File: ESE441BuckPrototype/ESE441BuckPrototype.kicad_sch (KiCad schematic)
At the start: 0 parts

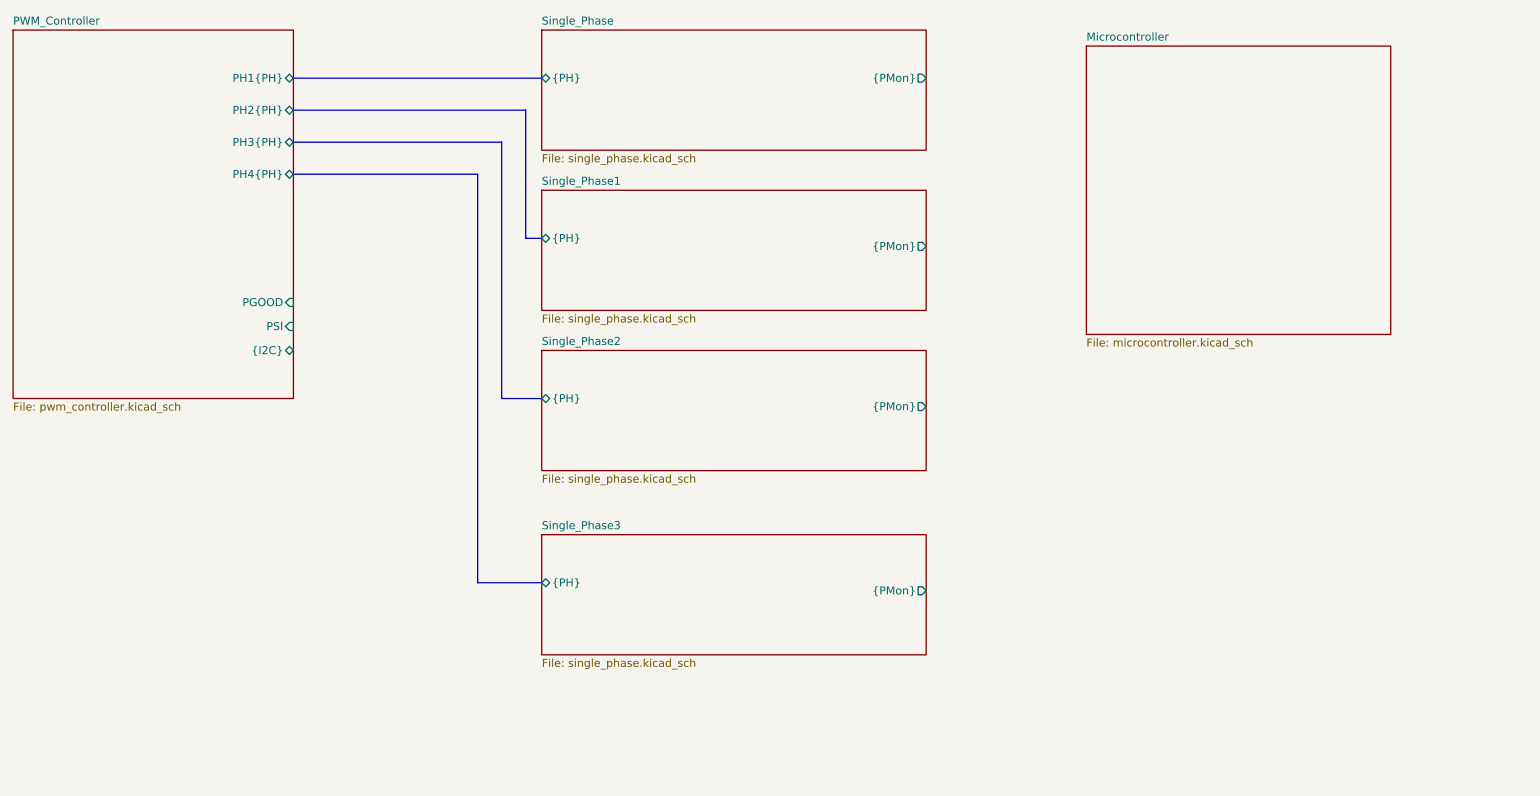
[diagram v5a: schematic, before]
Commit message: Wire up microcontroller to phases and PWM controller
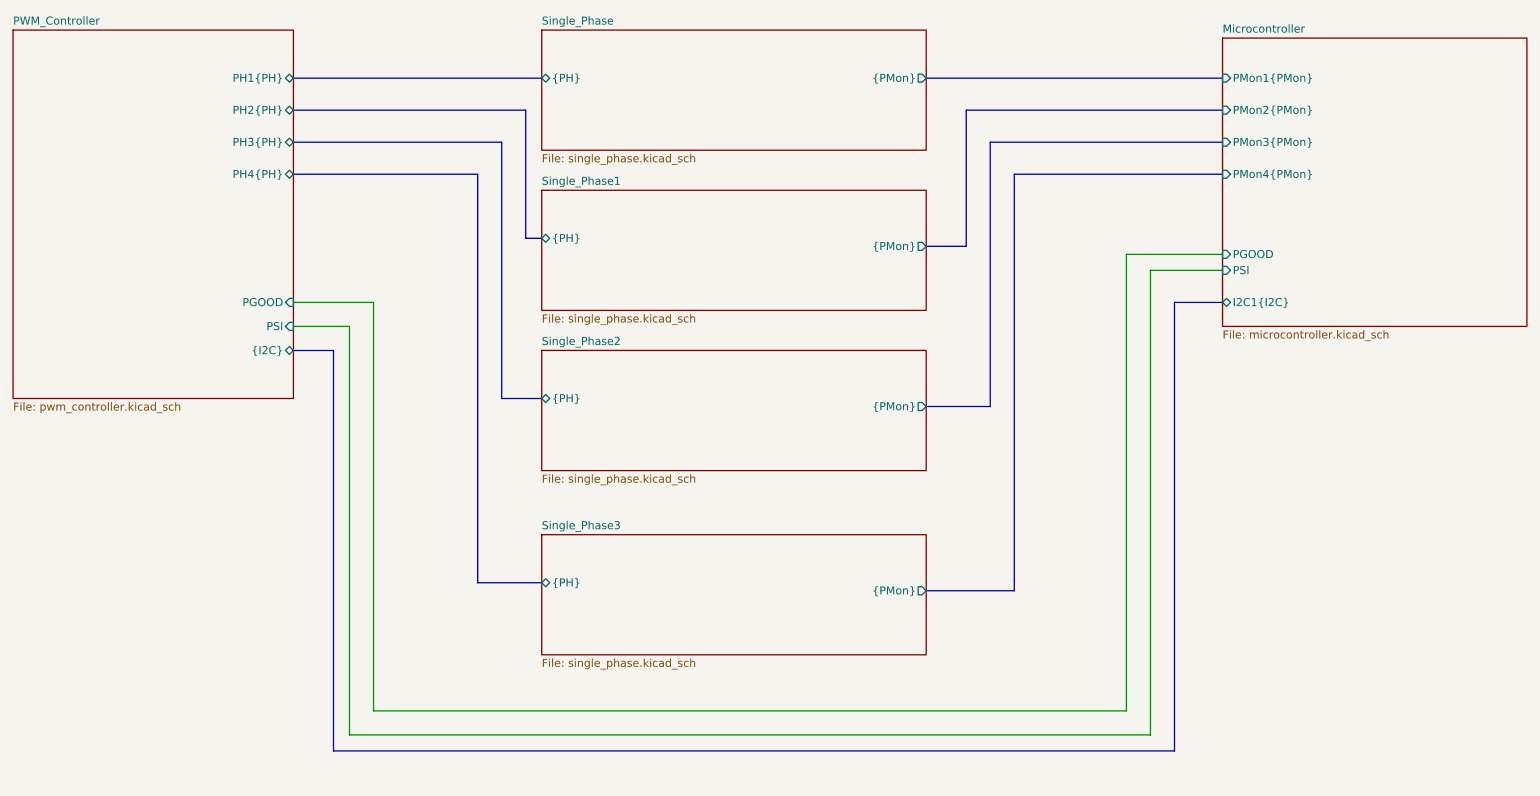
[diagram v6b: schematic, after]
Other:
- sheet Microcontroller ports: added I2C1{I2C}, PGOOD, PMon1{PMon}, PMon2{PMon}, PMon3{PMon}, PMon4{PMon}, PSI; removed none
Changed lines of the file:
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@@
+    (stroke (width 0) (type default) (color 0 0 0 0))
+  )
+  (wire (pts (xy 212.09 142.24) (xy 212.09 69.85))
     (stroke (width 0) (type default) (color 0 0 0 0))
   )
@@
     (stroke (width 0) (type default) (color 0 0 0 0))
   )
+  (bus (pts (xy 86.36 85.09) (xy 80.01 85.09))
+    (stroke (width 0) (type default) (color 0 0 0 0))
+  )
   (bus (pts (xy 109.22 121.92) (xy 119.38 121.92))
     (stroke (width 0) (type default) (color 0 0 0 0))
   )
+  (bus (pts (xy 186.69 46.99) (xy 227.33 46.99))
+    (stroke (width 0) (type default) (color 0 0 0 0))
+  )
+  (bus (pts (xy 180.34 68.58) (xy 186.69 68.58))
+    (stroke (width 0) (type default) (color 0 0 0 0))
+  )
+  (bus (pts (xy 180.34 41.91) (xy 227.33 41.91))
+    (stroke (width 0) (type default) (color 0 0 0 0))
+  )
+  (wire (pts (xy 227.33 72.39) (xy 215.9 72.39))
+    (stroke (width 0) (type default) (color 0 0 0 0))
+  )
+  (bus (pts (xy 186.69 68.58) (xy 186.69 46.99))
+    (stroke (width 0) (type default) (color 0 0 0 0))
+  )
+  (bus (pts (xy 194.31 123.19) (xy 194.31 57.15))
+    (stroke (width 0) (type default) (color 0 0 0 0))
+  )
+  (bus (pts (xy 227.33 52.07) (xy 190.5 52.07))
+    (stroke (width 0) (type default) (color 0 0 0 0))
+  )
+  (wire (pts (xy 215.9 72.39) (xy 215.9 146.05))
+    (stroke (width 0) (type default) (color 0 0 0 0))
+  )
+  (bus (pts (xy 180.34 123.19) (xy 194.31 123.19))
+    (stroke (width 0) (type default) (color 0 0 0 0))
+  )
+  (wire (pts (xy 212.09 69.85) (xy 227.33 69.85))
+    (stroke (width 0) (type default) (color 0 0 0 0))
+  )
+  (bus (pts (xy 219.71 148.59) (xy 86.36 148.59))
+    (stroke (width 0) (type default) (color 0 0 0 0))
+  )
+  (bus (pts (xy 219.71 77.47) (xy 219.71 148.59))
+    (stroke (width 0) (type default) (color 0 0 0 0))
+  )
   (bus (pts (xy 80.01 41.91) (xy 119.38 41.91))
     (stroke (width 0) (type default) (color 0 0 0 0))
@@
     (stroke (width 0) (type default) (color 0 0 0 0))
   )
+  (wire (pts (xy 92.71 77.47) (xy 92.71 142.24))
+    (stroke (width 0) (type default) (color 0 0 0 0))
+  )
+  (wire (pts (xy 80.01 77.47) (xy 92.71 77.47))
+    (stroke (width 0) (type default) (color 0 0 0 0))
+  )
+  (bus (pts (xy 86.36 148.59) (xy 86.36 85.09))
+    (stroke (width 0) (type default) (color 0 0 0 0))
+  )
+  (wire (pts (xy 80.01 81.28) (xy 88.9 81.28))
+    (stroke (width 0) (type default) (color 0 0 0 0))
+  )
+  (bus (pts (xy 194.31 57.15) (xy 227.33 57.15))
+    (stroke (width 0) (type default) (color 0 0 0 0))
+  )
+  (bus (pts (xy 219.71 77.47) (xy 227.33 77.47))
+    (stroke (width 0) (type default) (color 0 0 0 0))
+  )
+  (wire (pts (xy 215.9 146.05) (xy 88.9 146.05))
+    (stroke (width 0) (type default) (color 0 0 0 0))
+  )
+  (wire (pts (xy 92.71 142.24) (xy 212.09 142.24))
+    (stroke (width 0) (type default) (color 0 0 0 0))
+  )
+  (bus (pts (xy 190.5 52.07) (xy 190.5 93.98))
+    (stroke (width 0) (type default) (color 0 0 0 0))
+  )
+  (wire (pts (xy 88.9 146.05) (xy 88.9 81.28))
+    (stroke (width 0) (type default) (color 0 0 0 0))
+  )
   (bus (pts (xy 116.84 46.99) (xy 116.84 67.31))
     (stroke (width 0) (type default) (color 0 0 0 0))
   )
+  (bus (pts (xy 180.34 93.98) (xy 190.5 93.98))
+    (stroke (width 0) (type default) (color 0 0 0 0))
+  )
   (sheet (at 119.38 114.3) (size 60.96 19.05) (fields_autoplaced)
     (stroke (width 0.1524) (type solid) (color 0 0 0 0))
@@
     )
   )
-  (sheet (at 205.74 36.83) (size 48.26 45.72) (fields_autoplaced)
-    (stroke (width 0.1524) (type solid) (color 0 0 0 0))
-    (fill (color 0 0 0 0.0000))
-    (property "Sheet name" "Microcontroller" (id 0) (at 205.74 36.1184 0)
-      (effects (font (size 1.27 1.27)) (justify left bottom))
-    )
-    (property "Sheet file" "microcontroller.kicad_sch" (id 1) (at 205.74 83.1346 0)
-      (effects (font (size 1.27 1.27)) (justify left top))
-    )
-  )
+  (sheet (at 227.33 35.56) (size 48.26 45.72) (fields_autoplaced)
+    (stroke (width 0.1524) (type solid) (color 0 0 0 0))
+    (fill (color 0 0 0 0.0000))
+    (property "Sheet name" "Microcontroller" (id 0) (at 227.33 34.8484 0)
+      (effects (font (size 1.27 1.27)) (justify left bottom))
+    )
+    (property "Sheet file" "microcontroller.kicad_sch" (id 1) (at 227.33 81.8646 0)
+      (effects (font (size 1.27 1.27)) (justify left top))
+    )
+    (pin "I2C1{I2C}" bidirectional (at 227.33 77.47 180)
+      (effects (font (size 1.27 1.27)) (justify left))
+    )
+    (pin "PMon1{PMon}" input (at 227.33 41.91 180)
+      (effects (font (size 1.27 1.27)) (justify left))
+    )
+    (pin "PGOOD" input (at 227.33 69.85 180)
+      (effects (font (size 1.27 1.27)) (justify left))
+    )
+    (pin "PSI" input (at 227.33 72.39 180)
+      (effects (font (size 1.27 1.27)) (justify left))
+    )
+    (pin "PMon4{PMon}" input (at 227.33 57.15 180)
+      (effects (font (size 1.27 1.27)) (justify left))
+    )
+    (pin "PMon3{PMon}" input (at 227.33 52.07 180)
+      (effects (font (size 1.27 1.27)) (justify left))
+    )
+    (pin "PMon2{PMon}" input (at 227.33 46.99 180)
+      (effects (font (size 1.27 1.27)) (justify left))
+    )
+  )

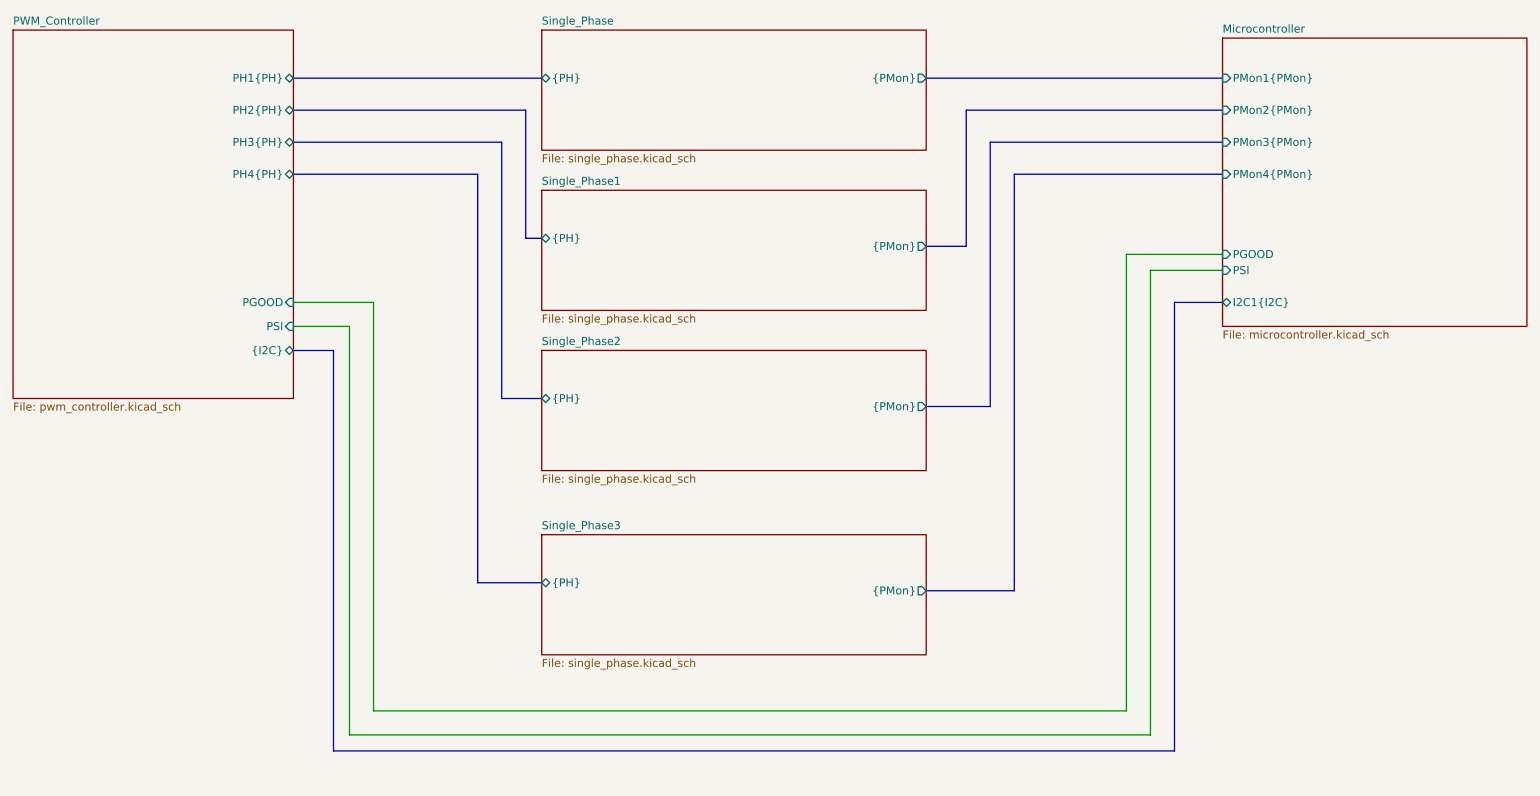
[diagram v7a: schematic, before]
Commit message: Add ALERT# monitoring and fix input/output sheet pins
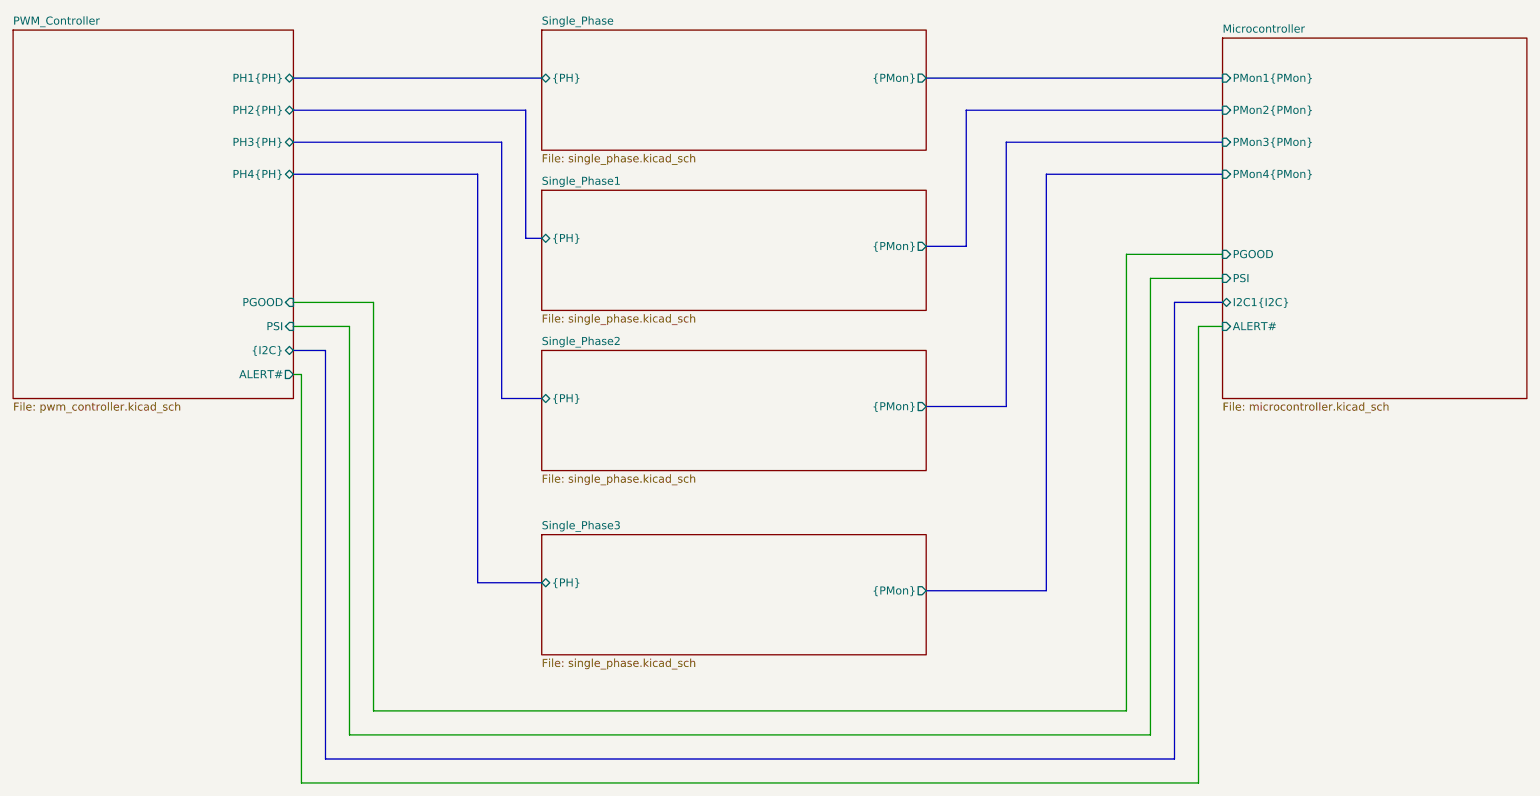
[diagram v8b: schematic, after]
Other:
- sheet Microcontroller ports: added ALERT#; removed none
- sheet PWM_Controller ports: added ALERT#; removed none
